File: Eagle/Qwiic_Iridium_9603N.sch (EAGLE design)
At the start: 58 parts, among them J1 SS4-10-3.50-X-D, J3 PTH, J6 ISP, J7 U.FL, Q1 DMG3415U-7, Q2 2N2222, U1 ATTINY84-ARDUINO, U2 LTC3225EDDB#TRMPBF

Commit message: Updates for V2 of the PCB
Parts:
- removed S1, S2: STANDOFF_ELECTRICALMCMASTER-95117A411, SparkFun-Electromechanical:STANDOFF_ELECTRICALMCMASTER-95117A411
- added J8: (no value), SparkFun-Connectors:CONN_01PTH_NO_SILK_YES_STOP
- ANTENNA: device con-coax:SMA-142-0711-821/826 -> Qwiic_Iridium_9603N:SMA-142-0711-821/826
- J1: value SS4-10-3.50-X-D -> IRIDIUM_9603NIRIDIUM_9603N; device SS4-10-3.50-X-D:SS4-10-3.50-X-D -> Qwiic_Iridium_9603N:IRIDIUM_9603NIRIDIUM_9603N
- U2: device LTC_By_element14_Batch_1:LTC3225EDDB-TRMPBFDFN300X200-10L -> Qwiic_Iridium_9603N:LTC3225EDDB-TRMPBFDFN300X200-10L
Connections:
- net EXT_PWR: now also J1.EXT_PWR_1, J1.EXT_PWR_2, J8.1; no longer J1.1, J1.2
- net GND: now also J1.DTR, J1.EXT_GND_3, J1.EXT_GND_4, J1.HOLE1, J1.HOLE2, J1.RTS, J1.SIG_GND_15, J1.SIG_GND_18, J1.SIG_GND_8; no longer J1.13, J1.14, J1.15, J1.18, J1.3, J1.4, J1.8, S1.P$1, S2.P$1, U2.GND_2
- net NA: now also J1.NET_AVAIL; no longer J1.19
- net ON_OFF: now also J1.ON/!OFF!; no longer J1.5
- net RI: now also J1.RING_INDICATOR; no longer J1.12
- net RX(OUT): now also J1.RX(OUT); no longer J1.7
- net TX(IN): now also J1.TX(IN); no longer J1.6
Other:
- note removed: "Connector for Iridium 9603"
- note removed: "DF_CTS (OUT)"
- note removed: "DF_DCD (OUT)"
- note removed: "DF_DSR (OUT)"
- note removed: "DF_DTR (IN)"
- note removed: "DF_RI (OUT)"
- note removed: "DF_RTS (IN)"
- note removed: "DF_S_RX (OUT)"
- note removed: "DF_S_TX (IN)"
- note removed: "EXT_GND"
- note removed: "Mounting holes for Iridium 9603 2 x McMaster 95117A411 Press-In Nuts for 1.55mm PCB"
- note removed: "Network_Available"
- note removed: "ON/OFF"
- note removed: "Reserved"
- note removed: "SIG_GND"
- note removed: "SUPPLY_OUT"
- moved on the sheet: ANTENNA, C1, C2, C3, C4, C5, C6, C7, D1, D2, D3, J2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

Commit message: Substantial update after testing the PCB
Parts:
- ANTENNA: value SMA-142-0711-821/826 -> SMA-; device Qwiic_Iridium_9603N:SMA-142-0711-821/826 -> Qwiic_Iridium_9603N:SMA-
- JP1: device SparkFun-Passives:JUMPER-PAD-3-2OF3_NC_BY_TRACE_LARGE -> Qwiic_Iridium_9603N:JUMPER-PAD-3-2OF3_NC_BY_TRACE_LARGE
- U1: value ATTINY84-ARDUINO -> ATTINY841-ARDUINO; device SparkFun-IC-Microcontroller:ATTINY84-ARDUINO -> Qwiic_Iridium_9603N:ATTINY841-ARDUINO
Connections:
- net !SHDN: now also U1.(XTAL1/A10)10; no longer U1.(XTAL1)10
- net MISO: now also U1.(MISO/A5)5; no longer U1.(TX/MISO/A5)~5
- net NA: now also U1.(A7)7; no longer U1.(A7)~7
- net ON_OFF: now also U1.(A0)0; no longer U1.(A2)2
- net PGOOD: now also U1.(A8)8; no longer U1.(XTAL2)9
- net RI: now also U1.(INT0/XTAL2/A9)9; no longer U1.(INT0)~8
- net RX(OUT): now also U1.(RXD0/A2)2; no longer U1.(A1)1
- net SDA: now also U1.(SDA/MOSI/A6)6; no longer U1.(RX/SDA/MOSI/A6)~6
- net TX(IN): now also U1.(TXD0/A1)1; no longer U1.(A0)0
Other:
- note added: "V2"
- note removed: "X10"
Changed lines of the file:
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@@
 <part name="SUPPLY19" library="SparkFun-PowerSymbols" library_urn="urn:adsk.eagle:library:530" deviceset="3.3V" device=""/>
 <part name="J5" library="SparkFun-Connectors" deviceset="CONN_01" device="PTH_NO_SILK_YES_STOP"/>
-<part name="U1" library="SparkFun-IC-Microcontroller" deviceset="ATTINY84-ARDUINO" device=""/>
+<part name="U1" library="Qwiic_Iridium_9603N" deviceset="ATTINY841-ARDUINO" device=""/>
 <part name="JP2" library="SparkFun-Jumpers" library_urn="urn:adsk.eagle:library:528" deviceset="JUMPER-SMT_3_2-NC_TRACE" device="_SILK" package3d_urn="urn:adsk.eagle:package:39289/1" value="JUMPER-SMT_3_2-NC_TRACE_SILK"/>
 <part name="J6" library="SparkFun-Connectors" deviceset="AVR_SPI_PROG_3X2" device="TESTPOINTS" value="ISP"/>
@@
 <part name="U$53" library="microbuilder" deviceset="GND" device=""/>
 <part name="C4" library="SparkFun-Capacitors" library_urn="urn:adsk.eagle:library:510" deviceset="0.22UF" device="-0603-25V-10%" package3d_urn="urn:adsk.eagle:package:37414/1" value="0.22uF"/>
-<part name="JP1" library="SparkFun-Passives" deviceset="JUMPER-PAD-3-2OF3_NC_BY_TRACE" device="_LARGE" value=""/>
+<part name="JP1" library="Qwiic_Iridium_9603N" deviceset="JUMPER-PAD-3-2OF3_NC_BY_TRACE" device="_LARGE" value="JUMPER-PAD-3-2OF3_NC_BY_TRACE_LARGE"/>
 <part name="Q1" library="microbuilder" deviceset="MOSFET-P" device="WIDE" value="DMG3415U-7 "/>
 <part name="Q2" library="transistor" deviceset="*-NPN-" device="SOT23-BEC" technology="MMBT2222ALT1" value="2N2222"/>
@@
 <part name="GND27" library="SparkFun-PowerSymbols" library_urn="urn:adsk.eagle:library:530" deviceset="GND" device=""/>
 <part name="J7" library="SparkFun-Connectors" deviceset="U.FL2PIN" device="" value="U.FL"/>
-<part name="ANTENNA" library="Qwiic_Iridium_9603N" deviceset="SMA-" device="142-0711-821/826"/>
+<part name="ANTENNA" library="Qwiic_Iridium_9603N" deviceset="SMA-" device="" value="SMA-"/>
 <part name="SUPPLY5" library="SparkFun-PowerSymbols" library_urn="urn:adsk.eagle:library:530" deviceset="3.3V" device=""/>
 <part name="GND1" library="SparkFun-PowerSymbols" library_urn="urn:adsk.eagle:library:530" deviceset="GND" device=""/>
@@
 Based on the Qwiic MP3 Trigger
 and Qwiic GPS-RTK2 by N. Seidle</text>
-<text x="237.744" y="7.366" size="2.54" layer="94">X10</text>
+<text x="237.744" y="7.366" size="2.54" layer="94">V2</text>
 <text x="26.543" y="141.351" size="1.778" layer="97" rot="R90">Power</text>
 <text x="38.608" y="49.784" size="1.778" layer="97" align="center">7-Bit Unshifted I2C
@@
 <attribute name="NAME" x="104.14" y="15.748" size="1.778" layer="95" font="vector"/>
 </instance>
-<instance part="U1" gate="U1" x="38.1" y="76.2" smashed="yes">
+<instance part="U1" gate="G$1" x="38.1" y="76.2" smashed="yes">
 <attribute name="NAME" x="22.86" y="94.742" size="1.778" layer="95"/>
 <attribute name="VALUE" x="22.86" y="55.88" size="1.778" layer="96"/>
@@
 <instance part="JP1" gate="G$1" x="157.48" y="119.38" smashed="yes" rot="R270">
 <attribute name="NAME" x="157.861" y="116.84" size="1.778" layer="95" rot="R270"/>
-<attribute name="VALUE" x="155.575" y="116.84" size="1.778" layer="96" rot="R270"/>
 </instance>
 <instance part="Q1" gate="G$1" x="210.82" y="177.8" smashed="yes" rot="R90">
@@
 <wire x1="17.78" y1="91.44" x2="17.78" y2="93.98" width="0.1524" layer="91"/>
 <pinref part="SUPPLY17" gate="G$1" pin="3.3V"/>
-<pinref part="U1" gate="U1" pin="VCC"/>
+<pinref part="U1" gate="G$1" pin="VCC"/>
 </segment>
 <segment>
@@
 <wire x1="17.78" y1="60.96" x2="17.78" y2="58.42" width="0.1524" layer="91"/>
 <pinref part="GND13" gate="1" pin="GND"/>
-<pinref part="U1" gate="U1" pin="GND"/>
+<pinref part="U1" gate="G$1" pin="GND"/>
 </segment>
 <segment>
@@
 <wire x1="88.9" y1="78.74" x2="88.9" y2="71.12" width="0.1524" layer="91"/>
 <junction x="88.9" y="71.12"/>
-<pinref part="U1" gate="U1" pin="(SCL/SCK/A4)4"/>
+<pinref part="U1" gate="G$1" pin="(SCL/SCK/A4)4"/>
 </segment>
 <segment>
@@
 <wire x1="73.66" y1="78.74" x2="73.66" y2="76.2" width="0.1524" layer="91"/>
 <junction x="73.66" y="76.2"/>
-<pinref part="U1" gate="U1" pin="(RX/SDA/MOSI/A6)~6"/>
+<pinref part="U1" gate="G$1" pin="(SDA/MOSI/A6)6"/>
 </segment>
 <segment>
@@
 <junction x="58.42" y="91.44"/>
 <label x="63.5" y="91.44" size="1.27" layer="95" xref="yes"/>
-<pinref part="U1" gate="U1" pin="(!RESET!)11"/>
+<pinref part="U1" gate="G$1" pin="(!RESET!)11"/>
 </segment>
 <segment>
@@
 <wire x1="55.88" y1="73.66" x2="58.42" y2="73.66" width="0.1524" layer="91"/>
 <label x="58.42" y="73.66" size="1.27" layer="95" xref="yes"/>
-<pinref part="U1" gate="U1" pin="(TX/MISO/A5)~5"/>
+<pinref part="U1" gate="G$1" pin="(MISO/A5)5"/>
 </segment>
 <segment>
@@
 <net name="ON_OFF" class="0">
 <segment>
-<pinref part="U1" gate="U1" pin="(A2)2"/>
-<wire x1="55.88" y1="66.04" x2="58.42" y2="66.04" width="0.1524" layer="91"/>
-<label x="58.42" y="66.04" size="1.27" layer="95" xref="yes"/>
-</segment>
-<segment>
 <pinref part="J1" gate="G$1" pin="ON/!OFF!"/>
 <wire x1="182.88" y1="78.74" x2="175.26" y2="78.74" width="0.1524" layer="91"/>
 <label x="175.26" y="78.74" size="1.27" layer="95" rot="R180" xref="yes"/>
 </segment>
+<segment>
+<pinref part="U1" gate="G$1" pin="(A0)0"/>
+<wire x1="55.88" y1="60.96" x2="66.04" y2="60.96" width="0.1524" layer="91"/>
+<label x="66.04" y="60.96" size="1.27" layer="95" xref="yes"/>
+</segment>
 </net>
 <net name="RX(OUT)" class="0">
 <segment>
-<wire x1="66.04" y1="63.5" x2="58.42" y2="63.5" width="0.1524" layer="91"/>
-<label x="66.04" y="63.5" size="1.27" layer="95" xref="yes"/>
-<pinref part="U1" gate="U1" pin="(A1)1"/>
+<wire x1="66.04" y1="66.04" x2="58.42" y2="66.04" width="0.1524" layer="91"/>
+<label x="66.04" y="66.04" size="1.27" layer="95" xref="yes"/>
 <pinref part="RX" gate="G$1" pin="1"/>
-<wire x1="58.42" y1="63.5" x2="55.88" y2="63.5" width="0.1524" layer="91"/>
 <wire x1="78.74" y1="48.26" x2="58.42" y2="48.26" width="0.1524" layer="91"/>
-<wire x1="58.42" y1="48.26" x2="58.42" y2="63.5" width="0.1524" layer="91"/>
-<junction x="58.42" y="63.5"/>
+<wire x1="58.42" y1="48.26" x2="58.42" y2="66.04" width="0.1524" layer="91"/>
+<pinref part="U1" gate="G$1" pin="(RXD0/A2)2"/>
+<wire x1="55.88" y1="66.04" x2="58.42" y2="66.04" width="0.1524" layer="91"/>
+<junction x="58.42" y="66.04"/>
 </segment>
 <segment>
@@
 <net name="RI" class="0">
 <segment>
-<pinref part="U1" gate="U1" pin="(INT0)~8"/>
-<wire x1="55.88" y1="83.82" x2="58.42" y2="83.82" width="0.1524" layer="91"/>
-<label x="58.42" y="83.82" size="1.27" layer="95" xref="yes"/>
-</segment>
-<segment>
 <pinref part="J1" gate="G$1" pin="RING_INDICATOR"/>
 <wire x1="223.52" y1="71.12" x2="231.14" y2="71.12" width="0.1524" layer="91"/>
 <label x="231.14" y="71.12" size="1.27" layer="95" xref="yes"/>
 </segment>
+<segment>
+<pinref part="U1" gate="G$1" pin="(INT0/XTAL2/A9)9"/>
+<wire x1="55.88" y1="86.36" x2="58.42" y2="86.36" width="0.1524" layer="91"/>
+<label x="58.42" y="86.36" size="1.27" layer="95" xref="yes"/>
+</segment>
 </net>
 <net name="TX(IN)" class="0">
 <segment>
-<wire x1="55.88" y1="60.96" x2="60.96" y2="60.96" width="0.1524" layer="91"/>
-<label x="66.04" y="60.96" size="1.27" layer="95" xref="yes"/>
-<pinref part="U1" gate="U1" pin="(A0)0"/>
+<label x="66.04" y="63.5" size="1.27" layer="95" xref="yes"/>
 <pinref part="TX" gate="G$1" pin="1"/>
-<wire x1="60.96" y1="60.96" x2="66.04" y2="60.96" width="0.1524" layer="91"/>
+<wire x1="60.96" y1="63.5" x2="66.04" y2="63.5" width="0.1524" layer="91"/>
 <wire x1="78.74" y1="55.88" x2="60.96" y2="55.88" width="0.1524" layer="91"/>
-<wire x1="60.96" y1="55.88" x2="60.96" y2="60.96" width="0.1524" layer="91"/>
-<junction x="60.96" y="60.96"/>
+<wire x1="60.96" y1="55.88" x2="60.96" y2="63.5" width="0.1524" layer="91"/>
+<pinref part="U1" gate="G$1" pin="(TXD0/A1)1"/>
+<wire x1="55.88" y1="63.5" x2="60.96" y2="63.5" width="0.1524" layer="91"/>
+<junction x="60.96" y="63.5"/>
 </segment>
 <segment>
@@
 </segment>
 <segment>
-<pinref part="U1" gate="U1" pin="(XTAL1)10"/>
+<pinref part="U1" gate="G$1" pin="(XTAL1/A10)10"/>
 <wire x1="55.88" y1="88.9" x2="58.42" y2="88.9" width="0.1524" layer="91"/>
 <label x="58.42" y="88.9" size="1.27" layer="95" xref="yes"/>
@@
 </segment>
 <segment>
-<pinref part="U1" gate="U1" pin="(XTAL2)9"/>
-<wire x1="55.88" y1="86.36" x2="58.42" y2="86.36" width="0.1524" layer="91"/>
-<label x="58.42" y="86.36" size="1.27" layer="95" xref="yes"/>
+<pinref part="U1" gate="G$1" pin="(A8)8"/>
+<wire x1="55.88" y1="83.82" x2="58.42" y2="83.82" width="0.1524" layer="91"/>
+<label x="58.42" y="83.82" size="1.27" layer="95" xref="yes"/>
 </segment>
 </net>
@@
 </segment>
 <segment>
-<pinref part="U1" gate="U1" pin="(A3)3"/>
+<pinref part="U1" gate="G$1" pin="(A3)3"/>
 <wire x1="55.88" y1="68.58" x2="58.42" y2="68.58" width="0.1524" layer="91"/>
 <label x="58.42" y="68.58" size="1.27" layer="95" xref="yes"/>
@@
 <net name="NA" class="0">
 <segment>
-<pinref part="U1" gate="U1" pin="(A7)~7"/>
+<pinref part="U1" gate="G$1" pin="(A7)7"/>
 <wire x1="55.88" y1="78.74" x2="58.42" y2="78.74" width="0.1524" layer="91"/>
 <label x="58.42" y="78.74" size="1.27" layer="95" xref="yes"/>

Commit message: Added the ADM4210
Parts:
- removed Q2: 2N2222, transistor:MMBT2222ALT1-NPN-SOT23-BEC
- added C10: 0.22uF, SparkFun-Capacitors:0.22UF-0603-25V-10%
- added C9: 10nF, SparkFun-Capacitors:10NF-0603-50V-10%
- added R14: 10k, SparkFun-Resistors:10KOHM-0603-1/10W-1%
- added U3: ADM4210-1, ADM4210:ADM4210-1
- J1: value IRIDIUM_9603NIRIDIUM_9603N -> IRIDIUM_9603N; device Qwiic_Iridium_9603N:IRIDIUM_9603NIRIDIUM_9603N -> Qwiic_Iridium_9603N:IRIDIUM_9603N
- Q1: value DMG3415U-7 -> DMG3414U-7; device microbuilder:MOSFET-PWIDE -> DMG3414U-7:DMG3414U-7
- R10: value 1k -> 100; device SparkFun-Resistors:1KOHM-0603-1/10W-1% -> SparkFun-Resistors:100OHM-0603-1/10W-1%
- R11: value 10k -> 100; device SparkFun-Resistors:10KOHM-0603-1/10W-1% -> SparkFun-Resistors:100OHM-0603-1/10W-1%
- R9: value 10k -> 0.012 Ohm; device SparkFun-Resistors:10KOHM-0603-1/10W-1% -> SparkFun-Resistors:RESISTOR0603
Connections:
- removed net N$19: Q1.G, Q2.C, R9.2
- removed net N$20: Q2.B, R10.2
- new net N$12: Q1.G, R10.1
- new net N$13: R10.2, R11.1, U3.GATE
- new net N$14: C9.1, R11.2
- new net N$15: C10.1, U3.TIMER
- new net N$8: Q1.D, R9.1, U3.SENSE
- net EXT_PWR: now also Q1.S; no longer Q1.D
- net GND: now also C10.2, C9.2, R14.2, U3.GND; no longer Q2.E, R11.2
- net LTC3225_VOUT: now also R9.2, U3.VCC; no longer Q1.S, R9.1
- net PWR_EN: now also R14.1, U3.ON; no longer R10.1, R11.1
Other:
- note added: "Inrush Current Limit"
- note added: "Super- capacitor Charger"
- note added: "V3"
- note removed: "SuperCapacitor Charger"
- note removed: "V2"
- moved on the sheet: C2, C3, C4, C5, C6, JP1, R10, R11, R5, R6, R7, R8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

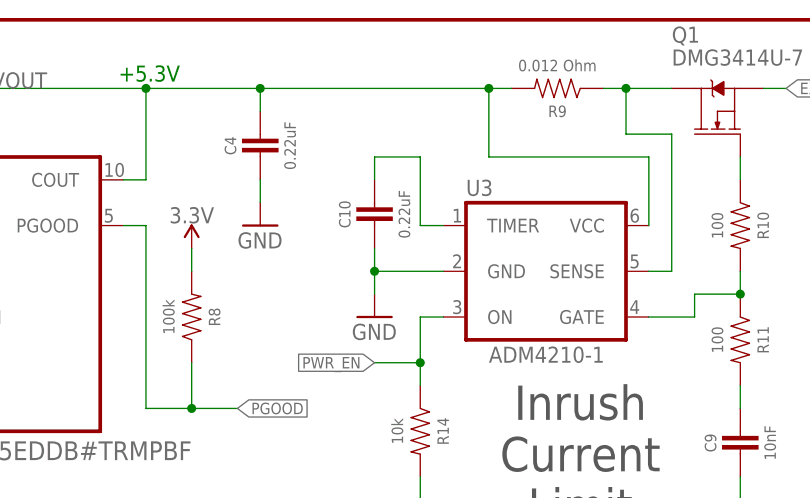
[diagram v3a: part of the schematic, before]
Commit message: Added assembly details for V3 of the PCB
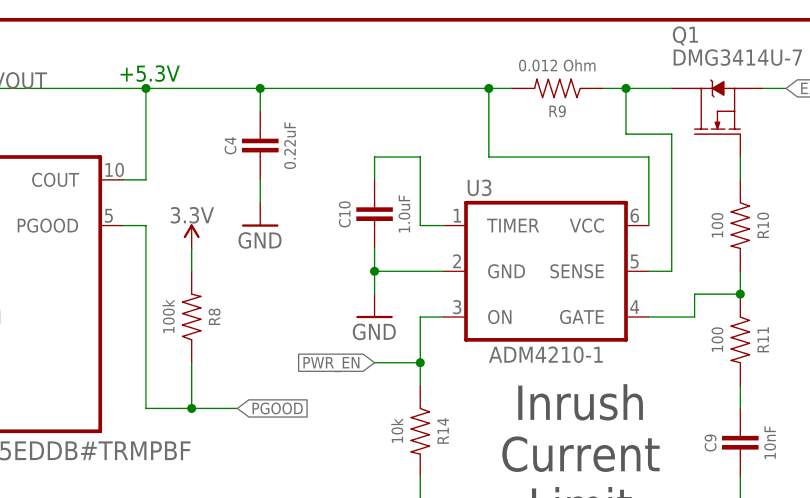
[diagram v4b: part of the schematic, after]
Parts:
- C10: value 0.22uF -> 1.0uF; device SparkFun-Capacitors:0.22UF-0603-25V-10% -> SparkFun-Capacitors:1.0UF-0603-16V-10%
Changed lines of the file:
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@@
 <part name="Q1" library="DMG3414U-7" deviceset="DMG3414U-7" device=""/>
 <part name="C9" library="SparkFun-Capacitors" library_urn="urn:adsk.eagle:library:510" deviceset="10NF" device="-0603-50V-10%" package3d_urn="urn:adsk.eagle:package:37414/1" value="10nF"/>
-<part name="C10" library="SparkFun-Capacitors" library_urn="urn:adsk.eagle:library:510" deviceset="0.22UF" device="-0603-25V-10%" package3d_urn="urn:adsk.eagle:package:37414/1" value="0.22uF"/>
+<part name="C10" library="SparkFun-Capacitors" library_urn="urn:adsk.eagle:library:510" deviceset="1.0UF" device="-0603-16V-10%" package3d_urn="urn:adsk.eagle:package:37414/1" value="1.0uF"/>
 <part name="R14" library="SparkFun-Resistors" library_urn="urn:adsk.eagle:library:532" deviceset="10KOHM" device="-0603-1/10W-1%" package3d_urn="urn:adsk.eagle:package:39650/1" value="10k"/>
 <part name="GND21" library="SparkFun-PowerSymbols" library_urn="urn:adsk.eagle:library:530" deviceset="GND" device=""/>
